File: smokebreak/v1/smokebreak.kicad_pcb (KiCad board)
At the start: 6 copper layers, 94 x 52 mm, 208 parts, among them J1 XT60 male, J2 XT30 male, J3 XT60 female, J4 XT30 female, J5 JST-XH 9, J6 SWD, J7 TFT1901 FPC, J8 USB-C, Q1 input FET, Q10 BC817, Q11 BSC070N10LS5, Q2 output FET, Q3 SUD50P10-43L, Q4 MMBTA42, Q5 BC817, Q6 MMBT5401, Q7 MMBT5401, Q8 2N7002, Q9 AO3400A, SW1 ON-OFF-(ON), SW2 Limit -, SW3 Limit +, U1 TPS48000, U10 SN74AHCT1G125, U11 USBLC6-2SC6, U12 LMV331, U2 INA181A2, U3 LMR36506R5, U4 TLV75533, U5 STM32G0B1RBT6, U6 DRV5032FA, U7 74LVC1G11, U8 LMV331, U9 SN74LVC1G74

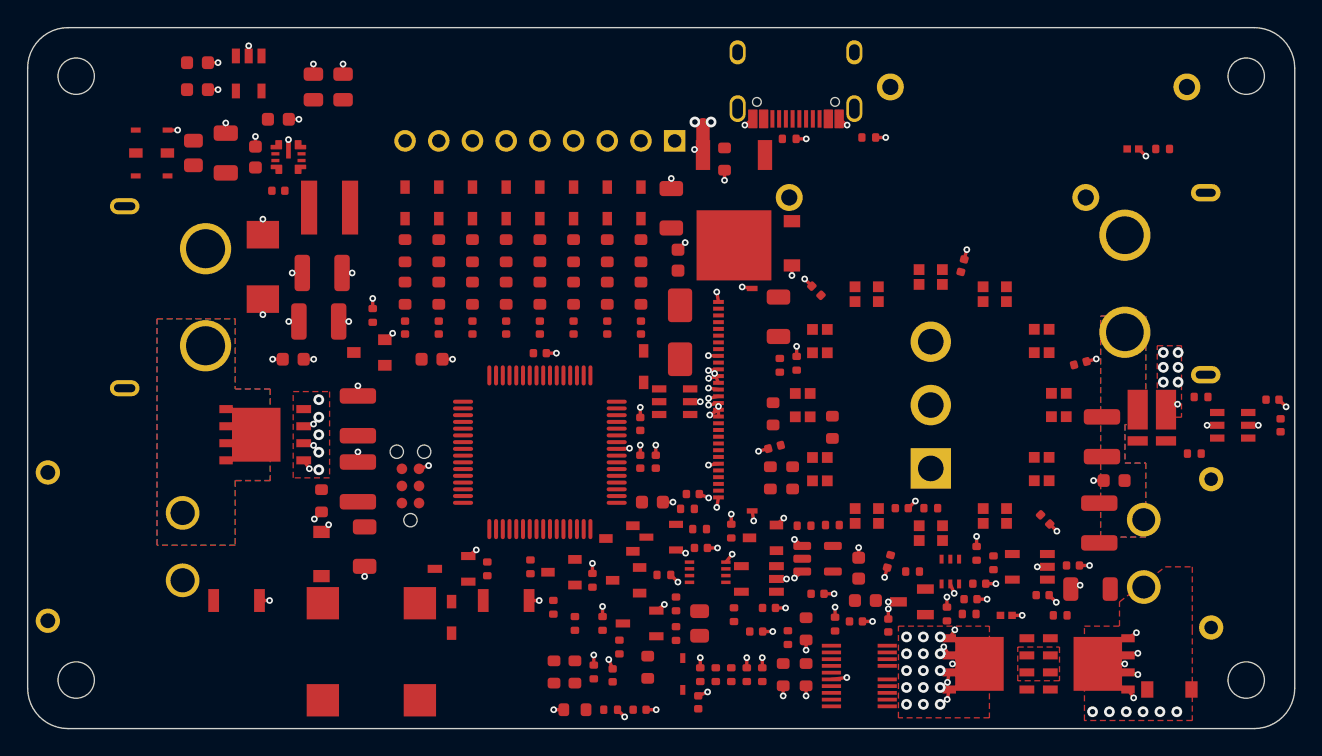
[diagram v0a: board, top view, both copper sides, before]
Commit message: smokebreak v1: TPS48000 above the FETs (gate over Q1's gate, SRC over the source copper), its passives around it, snubber inside the ring, comparator among the controller passives
Co-Authored-By: Claude Opus 5.5 <noreply@anthropic.com>
Claude-Session: https://claude.ai/code/session_01SBnFJLvm1wBa1jZy4RXnma
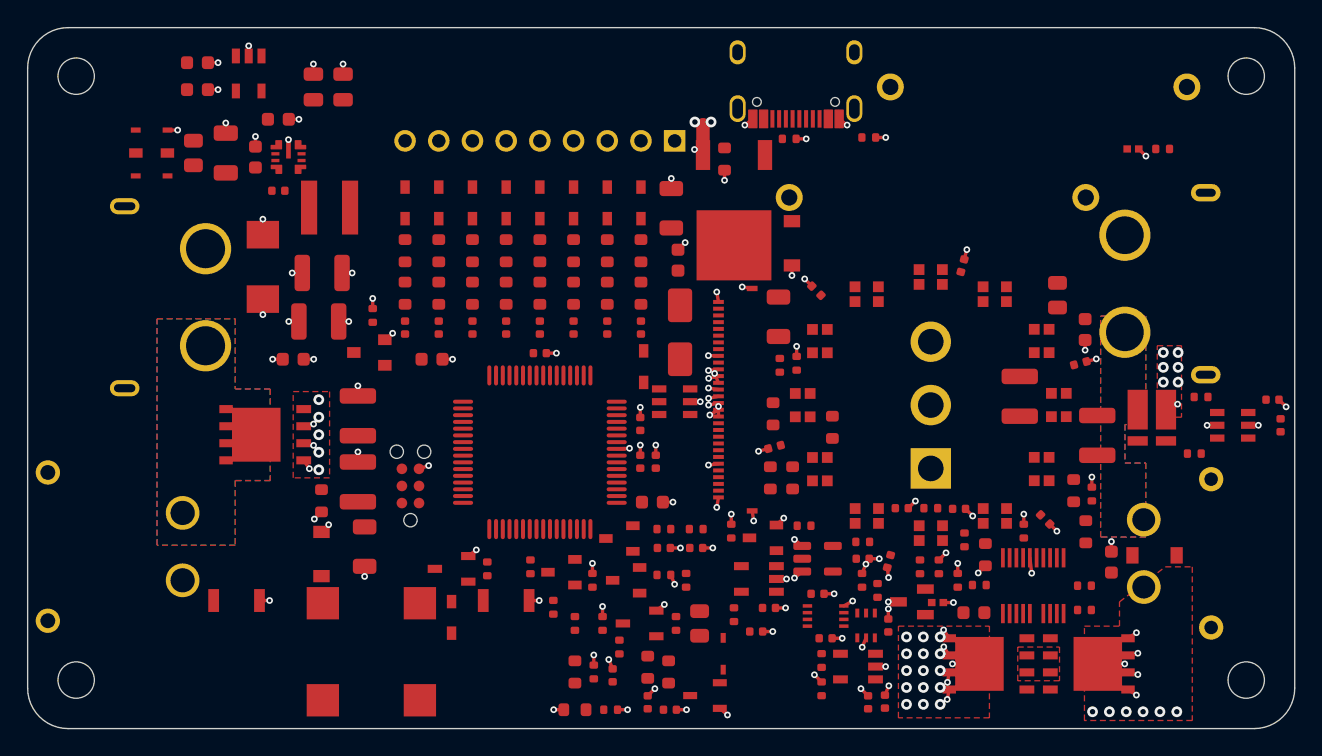
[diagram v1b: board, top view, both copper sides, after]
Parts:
- R68: footprint R_1206_3216Metric -> R_0805_2012Metric
- moved R2 24.1 mm to (177.6, 134.3)
- moved R1 22.0 mm to (178.5, 137.4)
- moved R68 21.9 mm to (176.4, 119.8), turned to 90 degrees
- moved R3 21.4 mm to (178.9, 134.6)
- moved C4 18.8 mm to (180.4, 139.7)
- moved C56 18.3 mm to (162.3, 150.1), turned to 90 degrees
- moved R4 17.4 mm to (171.1, 139.1)
- moved R10 16.3 mm to (167.6, 140.0)
- moved R11 16.1 mm to (166.2, 140.0)
- moved R9 16.1 mm to (169.0, 141.0)
- moved R71 15.3 mm to (158.9, 149.1)
- moved R8 15.0 mm to (169.5, 138.0)
- moved U12 14.7 mm to (161.6, 147.4)
- moved R70 14.7 mm to (158.9, 146.9)
- moved U1 14.5 mm to (174.6, 141.4), turned to 180 degrees
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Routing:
- net VIN: track 18.1 -> 16.6 mm, vias 36 -> 34
- net VOUT: track 6.50 -> 5.75 mm, vias 13 -> 12

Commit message: smokebreak v1: board state from the final pass in progress
Co-Authored-By: Claude Opus 5.5 <noreply@anthropic.com>
Claude-Session: https://claude.ai/code/session_01SBnFJLvm1wBa1jZy4RXnma
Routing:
- net +3V3: track 0.00 -> 303.0 mm, vias 0 -> 13
- net +5V: track 0.00 -> 233.3 mm, vias 0 -> 5
- net VOUT: track 5.75 -> 119.7 mm, vias 12 -> 17
- net VBUS: track 0.00 -> 98.5 mm, vias 0 -> 3
- net AUX: track 0.00 -> 92.1 mm, vias 0 -> 3
- net NTC_PRE: track 0.00 -> 67.1 mm, vias 0 -> 2
- net DIV_GND: track 0.00 -> 58.7 mm, vias 0 -> 5
- net I_SENSE: track 0.00 -> 47.1 mm, vias 0 -> 4
- net NTC_FET: track 0.00 -> 46.5 mm, vias 0 -> 3
- net GND: track 80.0 -> 125.0 mm, vias 116 -> 262
- net VOUT_LO: track 0.00 -> 44.5 mm, vias 0 -> 2
- net TPS_FLTGD: track 0.00 -> 42.1 mm, vias 0 -> 4
- net TOG_BIND: track 0.00 -> 41.2 mm, vias 0 -> 3
- net BTN_MINUS: track 0.00 -> 41.0 mm, vias 0 -> 2
- net TPS_FLT: track 0.00 -> 39.3 mm, vias 0 -> 3
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- added copper zone on B.Cu, net GND
- added copper zone on In2.Cu, net GND
- added copper zone on In3.Cu, net GND

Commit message: smokebreak v1: DRC 0 errors / 0 warnings, 2 joins open; gate side now routes BST and PU first
Co-Authored-By: Claude Opus 5.5 <noreply@anthropic.com>
Claude-Session: https://claude.ai/code/session_01SBnFJLvm1wBa1jZy4RXnma
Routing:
- net GATE: track 33.4 -> 21.2 mm, vias 2 -> 4
- net TPS_PU: track 10.3 -> 0.00 mm, vias 2 -> 0
- net TPS_BST: track 4.83 -> 0.00 mm
- net VIN: track 22.5 -> 27.2 mm, vias 34 -> 36
- net SRC: track 24.9 -> 21.0 mm, vias 5 -> 3
- net GND: track 125.0 -> 128.8 mm, vias 262 -> 264
- net VOUT: track 119.7 -> 117.8 mm
- net CDVDT: track 9.29 -> 7.65 mm

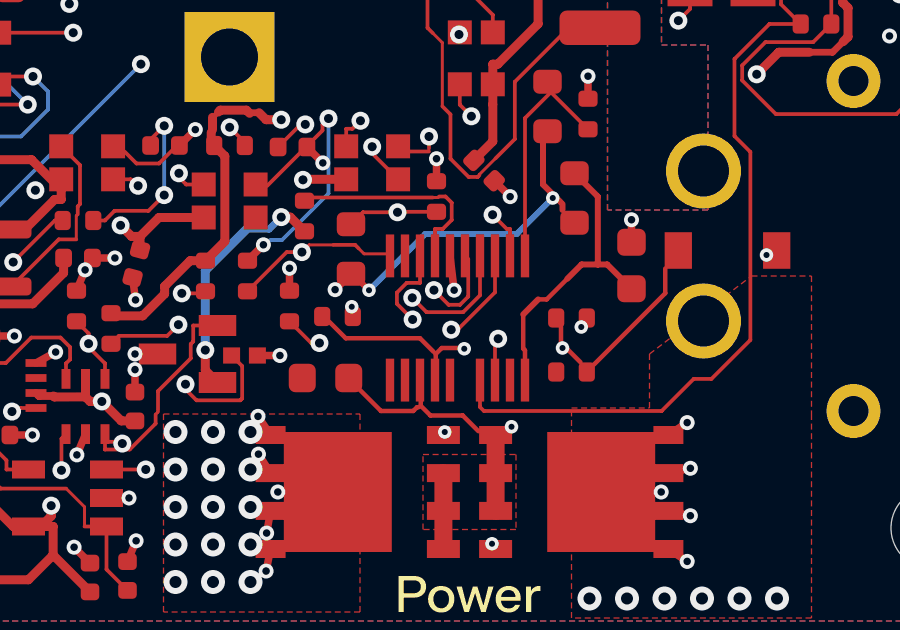
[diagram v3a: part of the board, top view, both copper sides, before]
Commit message: smokebreak v1: board with gate side rerouted, DRC 0 errors, 1 VIN link open
Co-Authored-By: Claude Opus 5.5 <noreply@anthropic.com>
Claude-Session: https://claude.ai/code/session_01SBnFJLvm1wBa1jZy4RXnma
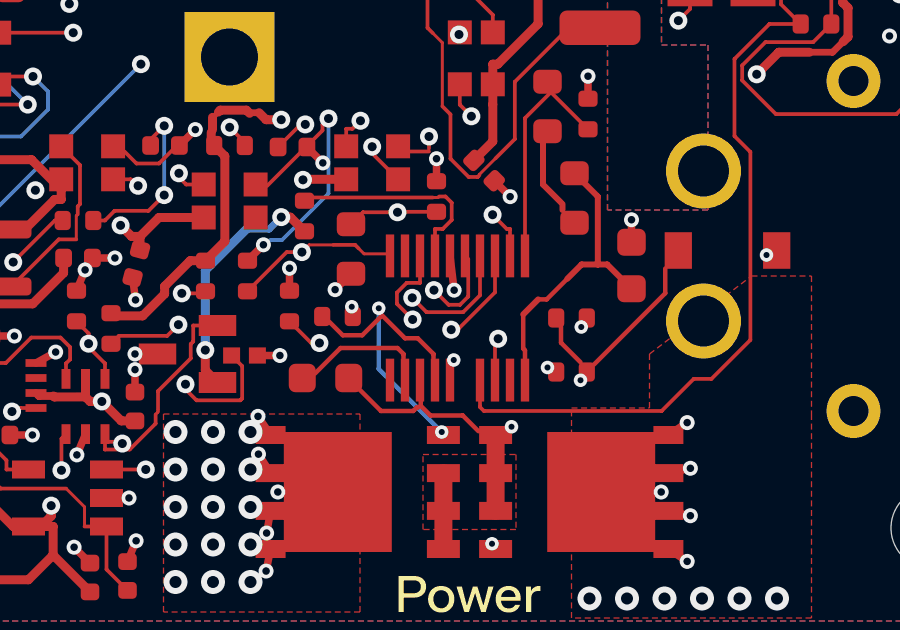
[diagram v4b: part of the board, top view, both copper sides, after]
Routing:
- net VIN: track 27.2 -> 19.0 mm, vias 36 -> 34
- net TPS_BST: track 0.00 -> 3.53 mm
- net TPS_PU: track 0.00 -> 3.23 mm, vias 0 -> 2
- net GATE: track 21.2 -> 24.1 mm
